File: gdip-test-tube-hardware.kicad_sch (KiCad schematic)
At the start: 38 parts, among them J1 USB_B, J2 USB_B, J3 Conn_01x06, J4 Conn_01x06, J5 Conn_01x06, J6 Screw_Terminal_01x02, Q1 S8050, Q2 S8050, SW1 SW_Push, SW2 SW_Push, U1 ESP32-S3-WROOM-1-N16R2, U2 AMS1117-3.3, U3 CP2102N-Axx-xQFN28, U4 USBLC6-2SC6, U5 USBLC6-2SC6

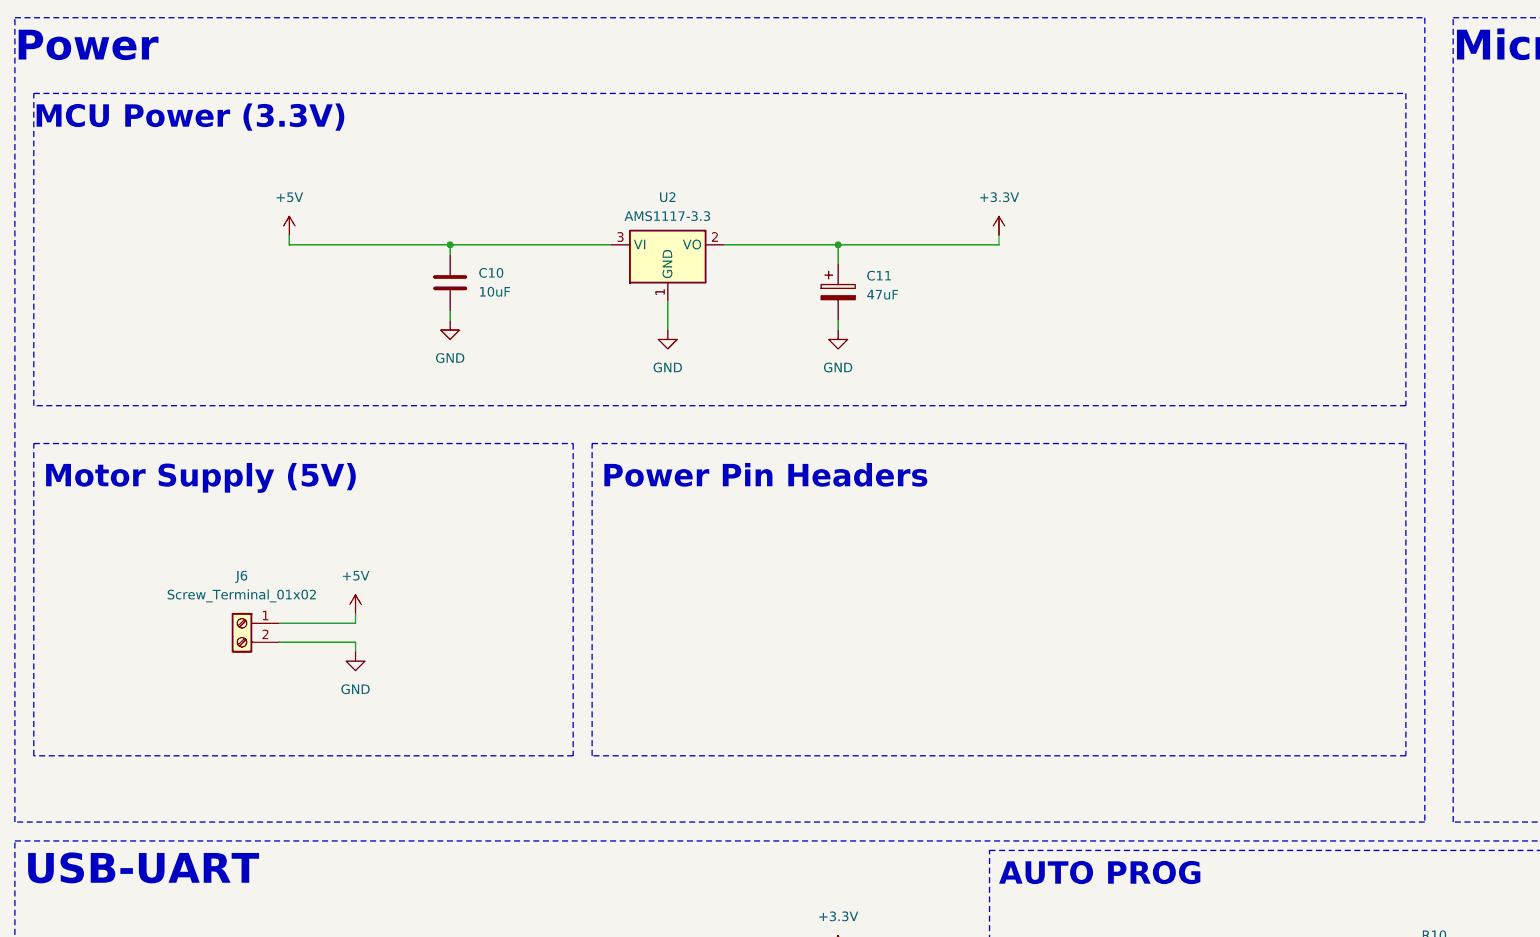
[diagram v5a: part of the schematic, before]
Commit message: Added LED for power supply indication.
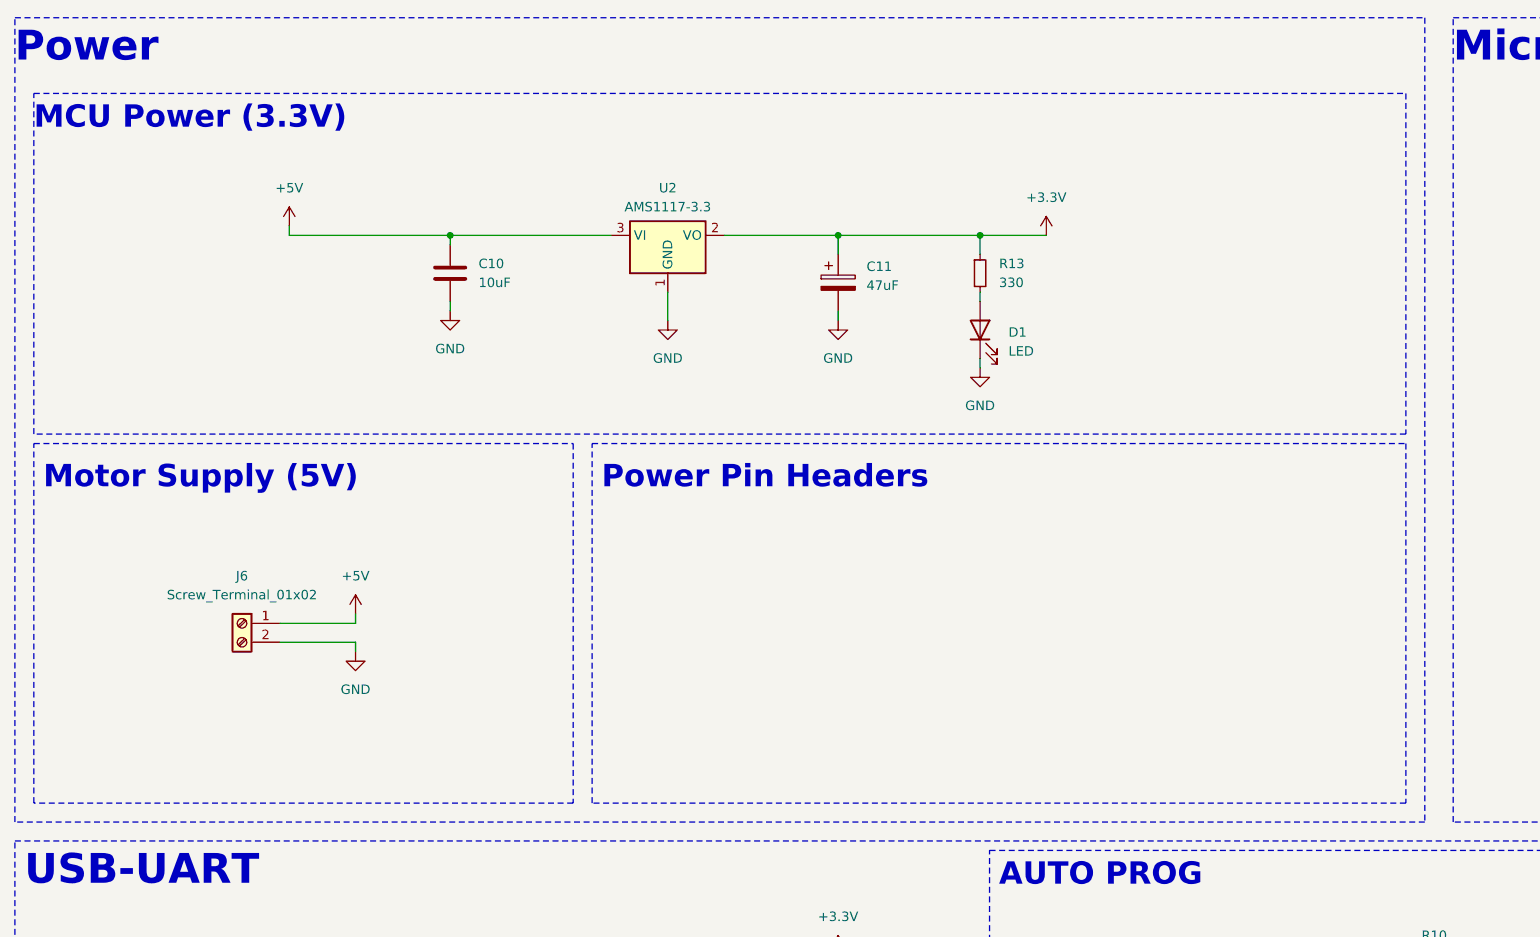
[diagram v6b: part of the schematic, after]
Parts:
- added D1: LED, symbol Device:LED
- added R13: 330, symbol Device:R_Small
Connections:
- net +3.3V: now also R13.1
- net GND: now also D1.1 (K)
- new net: D1.2 (A), R13.2
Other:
- moved on the sheet: C10, C11, U2

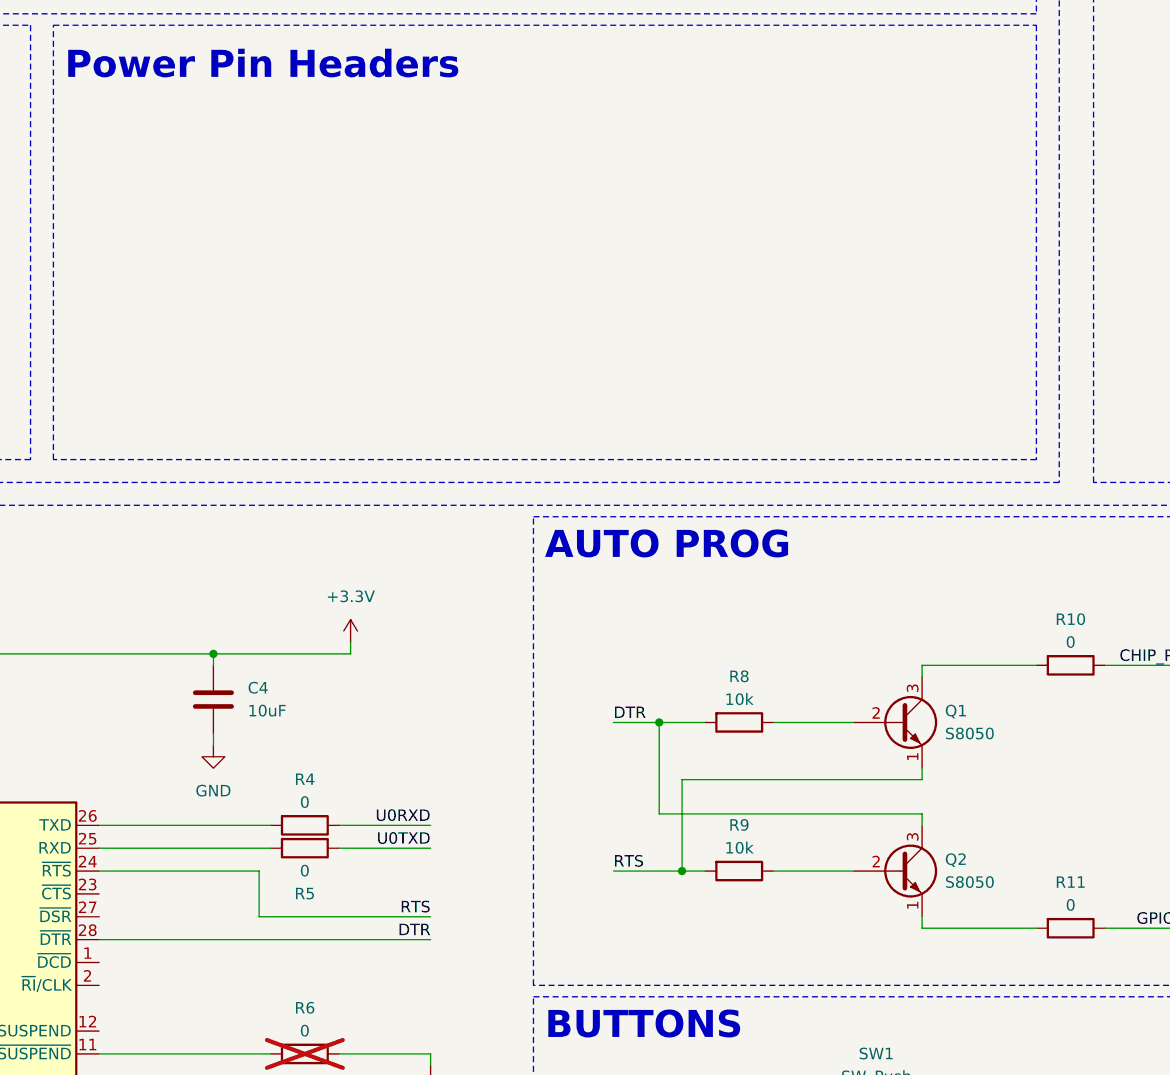
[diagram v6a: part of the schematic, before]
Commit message: Started inital layout, board with correct height and width, and main components placed.
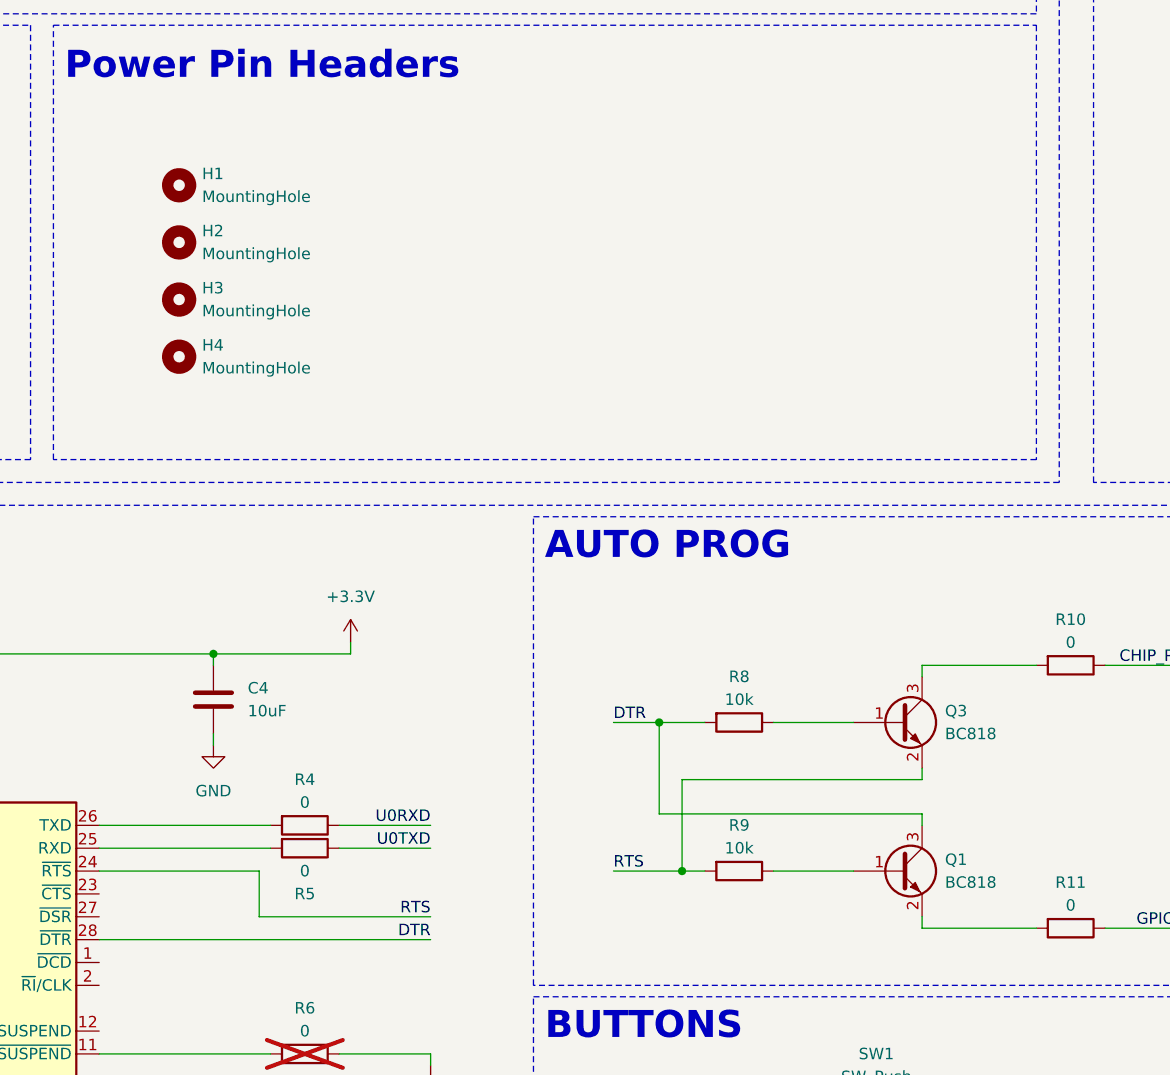
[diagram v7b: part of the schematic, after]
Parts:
- removed Q1, Q2: S8050, Package_TO_SOT_THT:TO-92_Inline, symbol Transistor_BJT:S8050
- added H1, H2, H3, H4: MountingHole, MountingHole:MountingHole_3.5mm, symbol Mechanical:MountingHole
- added Q1, Q3: BC818, Package_TO_SOT_SMD:SOT-23, symbol Transistor_BJT:BC818
- C1, C10, C11, C2, C3, C4, C5, C6, C7, C8, C9: footprint (none) -> Capacitor_SMD:C_0805_2012Metric
- D1: footprint (none) -> LED_SMD:LED_0805_2012Metric
- J1, J2: footprint (none) -> Connector_USB:USB_Mini-B_Wuerth_65100516121_Horizontal
- J3, J4, J5: footprint (none) -> Connector_PinHeader_2.54mm:PinHeader_1x06_P2.54mm_Vertical
- J6: footprint (none) -> gdip-test-tube:TE_282837-2
- R1, R10, R11, R12, R13, R2, R3, R4, R5, R6, R7, R8, R9: footprint (none) -> Resistor_SMD:R_0805_2012Metric
- SW1, SW2: footprint (none) -> Button_Switch_THT:SW_PUSH_6mm
- U1: footprint ESP32-S3-WROOM-1-N16R2:XCVR_ESP32-S3-WROOM-1-N16R2 -> gdip-test-tube:XCVR_ESP32-S3-WROOM-1-N16R2
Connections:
- net DTR: now also Q1.3 (C)
- net RTS: now also Q3.2 (E)
- net at R8.1: now also Q3.1 (B)
- net at R10.2: now also Q3.3 (C)
- net at R11.2: now also Q1.2 (E)
- net at R9.1: now also Q1.1 (B)

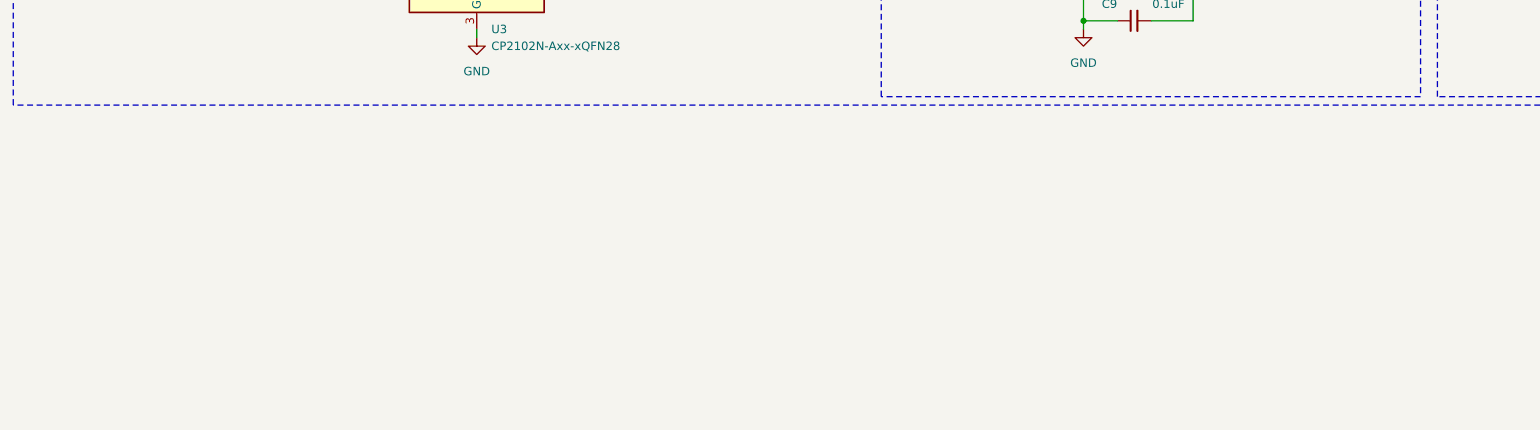
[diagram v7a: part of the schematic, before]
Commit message: Added buzzer circuit in.
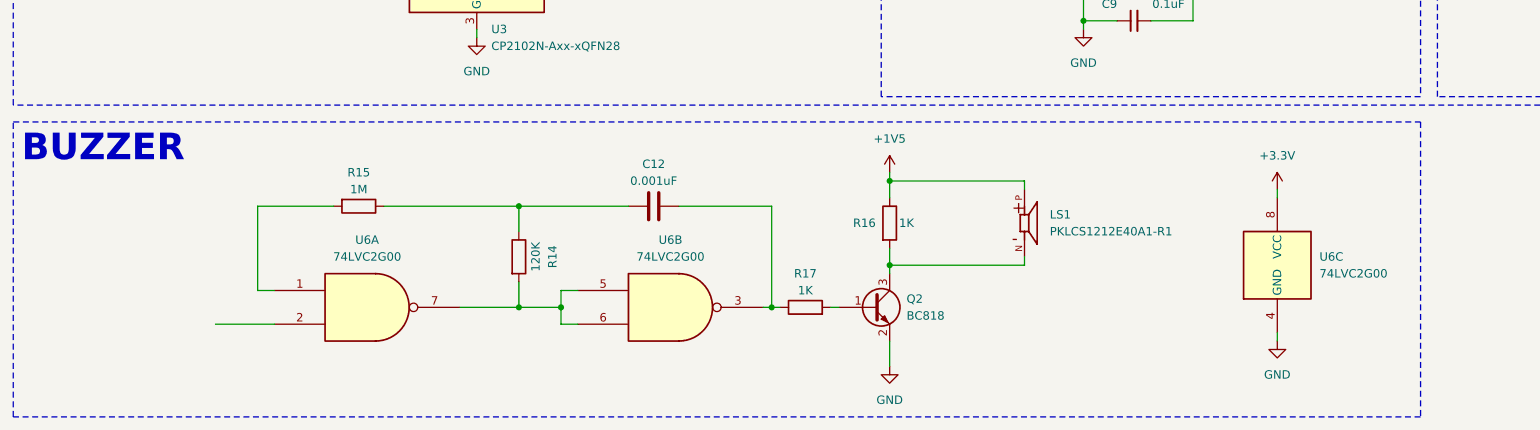
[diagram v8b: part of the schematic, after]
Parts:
- added C12: 0.001uF, Capacitor_SMD:C_0805_2012Metric, symbol Device:C
- added LS1: PKLCS1212E40A1-R1, PKLCS1212E40A1-R1:SPKR_PKLCS1212E40A1-R1, symbol gdip-test-tube:PKLCS1212E40A1-R1
- added Q2: BC818, Package_TO_SOT_SMD:SOT-23, symbol Transistor_BJT:BC818
- added R14: 120K, Resistor_SMD:R_0805_2012Metric, symbol Device:R
- added R15: 1M, Resistor_SMD:R_0805_2012Metric, symbol Device:R
- added R16, R17: 1K, Resistor_SMD:R_0805_2012Metric, symbol Device:R
- added U6: 74LVC2G00, Package_SO:VSSOP-8_2.4x2.1mm_P0.5mm, symbol 74xGxx:74LVC2G00
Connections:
- net +3.3V: now also U6.8 (VCC)
- net GND: now also Q2.2 (E), U6.4 (GND)
- new net: Q2.1 (B), R17.2
- new net: LS1.N, Q2.3 (C), R16.2
- new net: C12.1, R14.1, R15.1
- new net: R15.2, U6.1
- new net: R14.2, U6.5, U6.6, U6.7
- new net: C12.2, R17.1, U6.3
- new net +1V5: LS1.P, R16.1
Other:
- note added: "BUZZER"
